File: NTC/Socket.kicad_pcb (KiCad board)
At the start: 2 copper layers, 17.8 x 22.9 mm, 3 parts

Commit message: Added alternative DC/DC converter and Tube schematic
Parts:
- removed REF**: Pinbar_1-6-m-a, Nixie:Pinbar_1-6-m-a
- removed REF**: Pinbar_6-1-a, Nixie:Pinbar_1-6-m-b
- removed REF**: Gazotron IN-14, Nixie:Gazotron IN-14
- added H1: ~, Nixie:Gazotron IN-14, F.Cu at (127.0, 101.6)
- added X1: Conn_01x06_Pin, Nixie:Pinbar_1-6-m-a, F.Cu at (120.7, 92.7)
- added X2: Conn_01x06_Pin, Nixie:Pinbar_1-6-m-b, F.Cu at (120.7, 110.5)
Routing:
- net (no net): track 71.5 -> 0.00 mm
- net Net-(H1-9): track 0.00 -> 9.51 mm
- net Net-(H1-2): track 0.00 -> 9.51 mm
- net Net-(H1-3): track 0.00 -> 8.31 mm
- net Net-(H1-8): track 0.00 -> 8.31 mm
- net Net-(H1-1): track 0.00 -> 6.01 mm
- net Net-(H1-0): track 0.00 -> 5.92 mm
- net Net-(H1-7): track 0.00 -> 4.59 mm
- net Net-(H1-4): track 0.00 -> 4.59 mm
- net Net-(H1-DP_R): track 0.00 -> 4.38 mm
- net Net-(H1-+): track 0.00 -> 3.67 mm
- net Net-(H1-6): track 0.00 -> 3.35 mm
- net Net-(H1-5): track 0.00 -> 3.35 mm

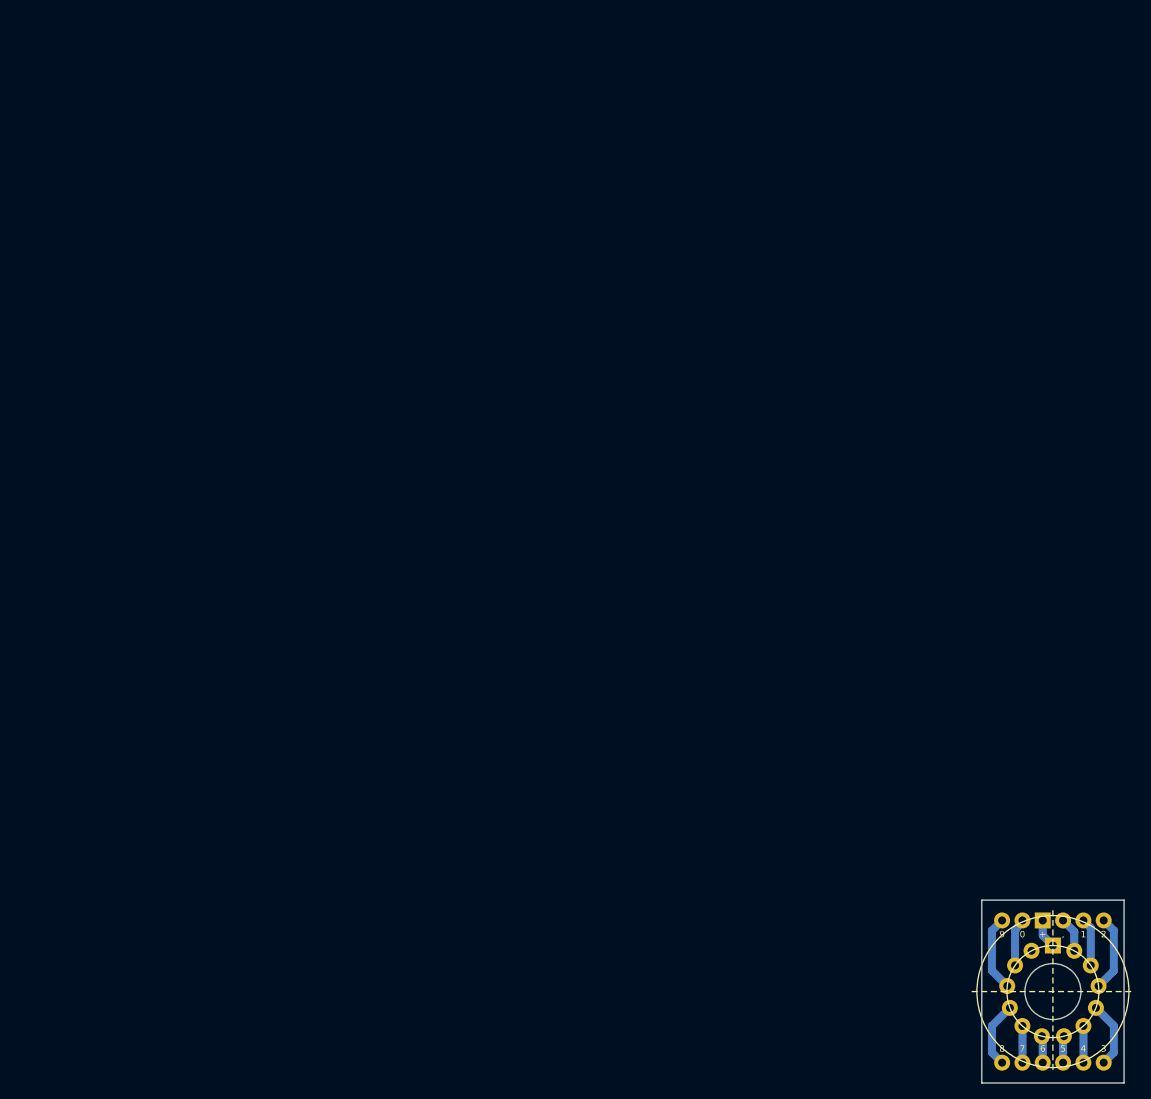
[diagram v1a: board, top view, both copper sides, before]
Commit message: Changed to 14pin socket
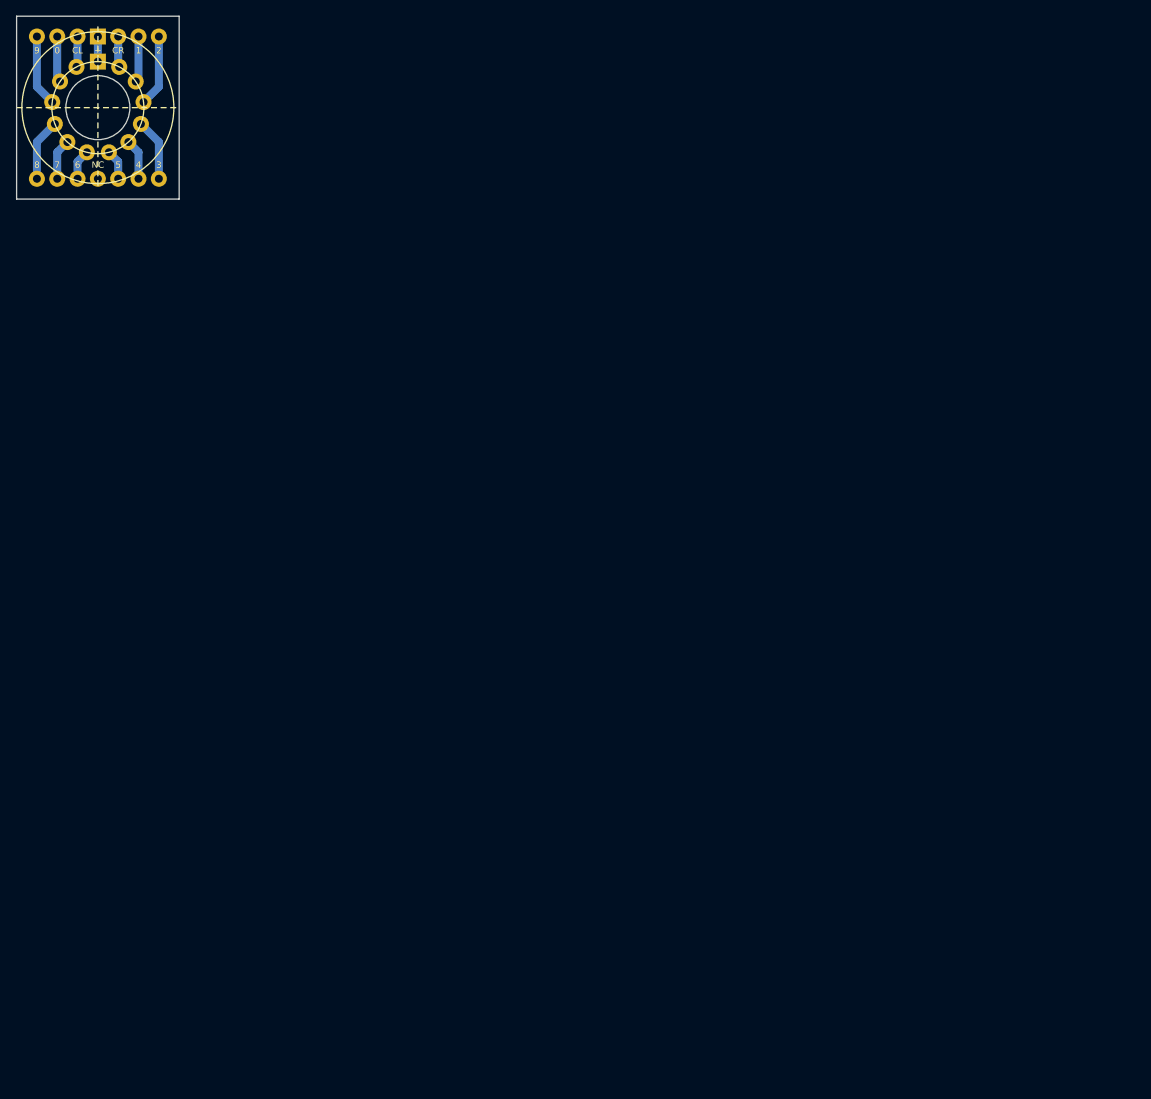
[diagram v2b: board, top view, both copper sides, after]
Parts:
- removed X2: Conn_01x06_Pin, Nixie:Pinbar_1-6-m-b
- X1: footprint Nixie:Pinbar_1-6-m-a -> Nixie:Pinbar_4-14-m
- moved H1 162.7 mm to (7.62, -8.89)
- moved X1 152.2 mm to (0.00, 0.00)
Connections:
- H1 pad 13: unconnected-(H1-DP_L-Pad13) -> Net-(H1-DP_L)
- X1 pad 3: Net-(H1-+) -> Net-(H1-DP_L)
- X1 pad 4: Net-(H1-DP_R) -> Net-(H1-+)
- X1 pad 5: Net-(H1-1) -> Net-(H1-DP_R)
- X1 pad 6: Net-(H1-2) -> Net-(H1-1)
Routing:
- net Net-(H1-DP_L): track 0.00 -> 3.85 mm
- net Net-(H1-3): track 8.31 -> 7.78 mm
- net Net-(H1-9): track 9.51 -> 8.99 mm
- net Net-(H1-8): track 8.31 -> 7.78 mm
- net Net-(H1-2): track 9.51 -> 8.99 mm
- net Net-(H1-+): track 3.67 -> 3.14 mm
- net Net-(H1-DP_R): track 4.38 -> 3.85 mm
- net Net-(H1-4): track 4.59 -> 5.11 mm
- net Net-(H1-7): track 4.59 -> 5.11 mm
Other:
- board size 17.8 x 22.9 mm -> 20.3 x 22.9 mm

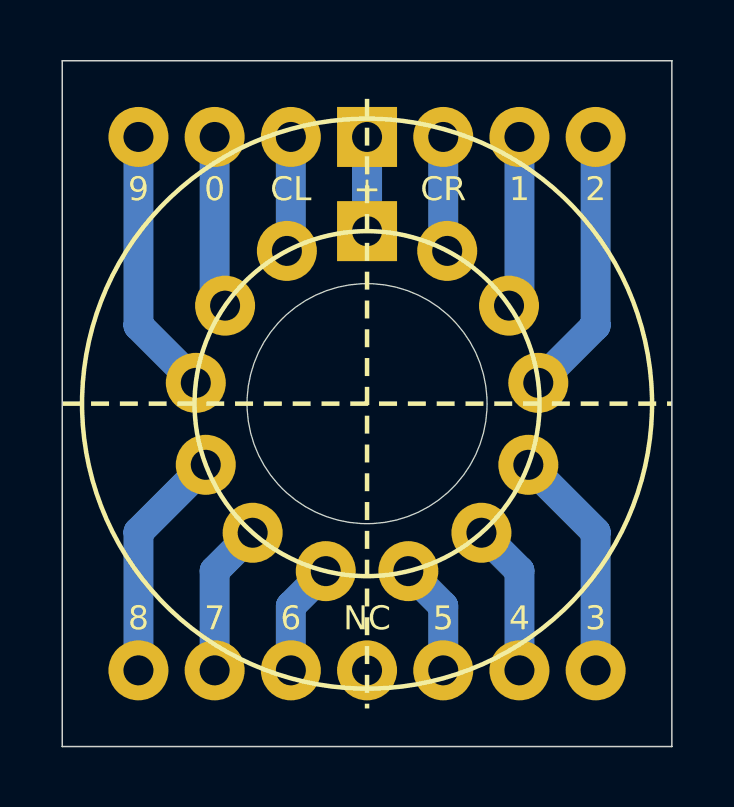
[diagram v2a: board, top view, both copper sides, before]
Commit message: Added GPS
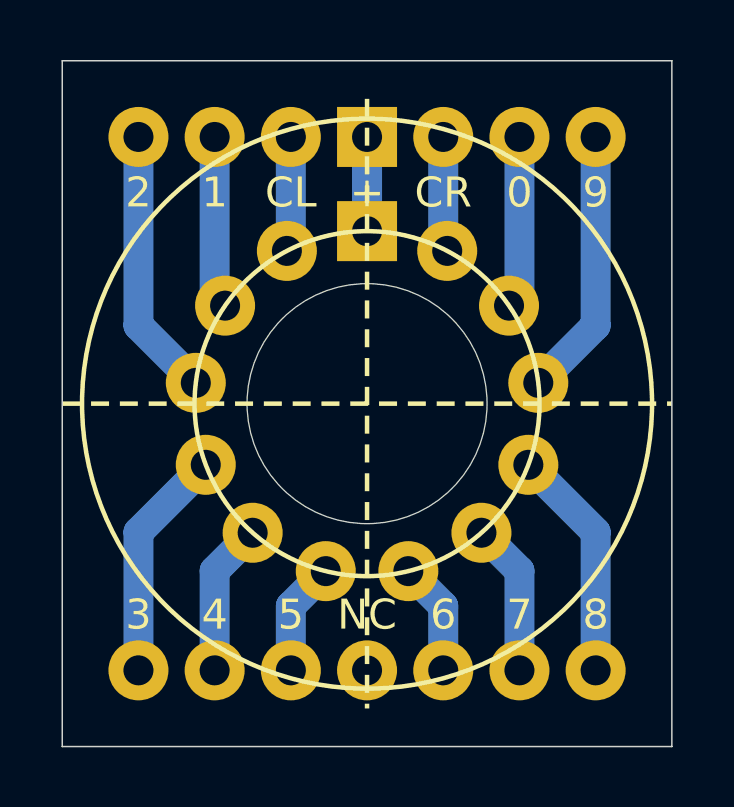
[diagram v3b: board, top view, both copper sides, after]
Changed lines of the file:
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@@
 			(layer "F.Mask"
 				(type "Top Solder Mask")
-				(color "Green")
+				(color "Blue")
 				(thickness 0.025)
 				(material "Elpemer AS 2467 SM-DG")
@@
 			(layer "B.Mask"
 				(type "Bottom Solder Mask")
-				(color "Green")
+				(color "Blue")
 				(thickness 0.025)
 				(material "Elpemer AS 2467 SM-DG")
@@
 			(layer "B.SilkS")
 		)
+		(fp_text user "CL"
+			(at 5.08 -16.51 0)
+			(unlocked yes)
+			(layer "F.SilkS")
+			(effects
+				(font
+					(size 1 1)
+					(thickness 0.15)
+				)
+				(justify top)
+			)
+		)
+		(fp_text user "9"
+			(at 15.24 -16.51 0)
+			(unlocked yes)
+			(layer "F.SilkS")
+			(effects
+				(font
+					(size 1 1)
+					(thickness 0.15)
+				)
+				(justify top)
+			)
+		)
+		(fp_text user "1"
+			(at 2.54 -16.51 0)
+			(unlocked yes)
+			(layer "F.SilkS")
+			(effects
+				(font
+					(size 1 1)
+					(thickness 0.15)
+				)
+				(justify top)
+			)
+		)
+		(fp_text user "2"
+			(at 0 -16.51 0)
+			(unlocked yes)
+			(layer "F.SilkS")
+			(effects
+				(font
+					(size 1 1)
+					(thickness 0.15)
+				)
+				(justify top)
+			)
+		)
 		(fp_text user "NC"
 			(at 7.62 -1.27 0)
@@
 			(effects
 				(font
-					(size 0.8 0.8)
+					(size 1 1)
 					(thickness 0.15)
 				)
@@
 			)
 		)
-		(fp_text user "1"
-			(at 12.7 -16.51 0)
-			(unlocked yes)
-			(layer "F.SilkS")
-			(effects
-				(font
-					(size 0.8 0.8)
+		(fp_text user "6"
+			(at 10.16 -1.27 0)
+			(unlocked yes)
+			(layer "F.SilkS")
+			(effects
+				(font
+					(size 1 1)
+					(thickness 0.15)
+				)
+				(justify bottom)
+			)
+		)
+		(fp_text user "4"
+			(at 2.54 -1.27 0)
+			(unlocked yes)
+			(layer "F.SilkS")
+			(effects
+				(font
+					(size 1 1)
+					(thickness 0.15)
+				)
+				(justify bottom)
+			)
+		)
+		(fp_text user "CR"
+			(at 10.16 -16.51 0)
+			(unlocked yes)
+			(layer "F.SilkS")
+			(effects
+				(font
+					(size 1 1)
 					(thickness 0.15)
 				)
 				(justify top)
-			)
-		)
-		(fp_text user "7"
-			(at 2.54 -1.27 0)
-			(unlocked yes)
-			(layer "F.SilkS")
-			(effects
-				(font
-					(size 0.8 0.8)
-					(thickness 0.15)
-				)
-				(justify bottom)
 			)
 		)
@@
 			(effects
 				(font
-					(size 0.8 0.8)
+					(size 1 1)
 					(thickness 0.15)
 				)
@@
 			)
 		)
+		(fp_text user "8"
+			(at 15.24 -1.27 0)
+			(unlocked yes)
+			(layer "F.SilkS")
+			(effects
+				(font
+					(size 1 1)
+					(thickness 0.15)
+				)
+				(justify bottom)
+			)
+		)
 		(fp_text user "3"
-			(at 15.24 -1.27 0)
-			(unlocked yes)
-			(layer "F.SilkS")
-			(effects
-				(font
-					(size 0.8 0.8)
+			(at 0 -1.27 0)
+			(unlocked yes)
+			(layer "F.SilkS")
+			(effects
+				(font
+					(size 1 1)
 					(thickness 0.15)
 				)
@@
 			)
 		)
-		(fp_text user "9"
-			(at 0 -16.51 0)
-			(unlocked yes)
-			(layer "F.SilkS")
-			(effects
-				(font
-					(size 0.8 0.8)
+		(fp_text user "7"
+			(at 12.7 -1.27 0)
+			(unlocked yes)
+			(layer "F.SilkS")
+			(effects
+				(font
+					(size 1 1)
+					(thickness 0.15)
+				)
+				(justify bottom)
+			)
+		)
+		(fp_text user "0"
+			(at 12.7 -16.51 0)
+			(unlocked yes)
+			(layer "F.SilkS")
+			(effects
+				(font
+					(size 1 1)
 					(thickness 0.15)
 				)
@@
 			)
 		)
-		(fp_text user "2"
-			(at 15.24 -16.51 0)
-			(unlocked yes)
-			(layer "F.SilkS")
-			(effects
-				(font
-					(size 0.8 0.8)
-					(thickness 0.15)
-				)
-				(justify top)
-			)
-		)
-		(fp_text user "8"
-			(at 0 -1.27 0)
-			(unlocked yes)
-			(layer "F.SilkS")
-			(effects
-				(font
-					(size 0.8 0.8)
-					(thickness 0.15)
-				)
-				(justify bottom)
-			)
-		)
-		(fp_text user "CR"
-			(at 10.16 -16.51 0)
-			(unlocked yes)
-			(layer "F.SilkS")
-			(effects
-				(font
-					(size 0.8 0.8)
-					(thickness 0.15)
-				)
-				(justify top)
-			)
-		)
 		(fp_text user "5"
-			(at 10.16 -1.27 0)
-			(unlocked yes)
-			(layer "F.SilkS")
-			(effects
-				(font
-					(size 0.8 0.8)
-					(thickness 0.15)
-				)
-				(justify bottom)
-			)
-		)
-		(fp_text user "4"
-			(at 12.7 -1.27 0)
-			(unlocked yes)
-			(layer "F.SilkS")
-			(effects
-				(font
-					(size 0.8 0.8)
-					(thickness 0.15)
-				)
-				(justify bottom)
-			)
-		)
-		(fp_text user "CL"
-			(at 5.08 -16.51 0)
-			(unlocked yes)
-			(layer "F.SilkS")
-			(effects
-				(font
-					(size 0.8 0.8)
-					(thickness 0.15)
-				)
-				(justify top)
-			)
-		)
-		(fp_text user "0"
-			(at 2.54 -16.51 0)
-			(unlocked yes)
-			(layer "F.SilkS")
-			(effects
-				(font
-					(size 0.8 0.8)
-					(thickness 0.15)
-				)
-				(justify top)
-			)
-		)
-		(fp_text user "6"
 			(at 5.08 -1.27 0)
 			(unlocked yes)
@@
 			(effects
 				(font
-					(size 0.8 0.8)
-					(thickness 0.15)
-				)
+					(size 1 1)
+					(thickness 0.15)
+				)
